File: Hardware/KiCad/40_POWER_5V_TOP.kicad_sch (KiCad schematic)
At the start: 0 parts

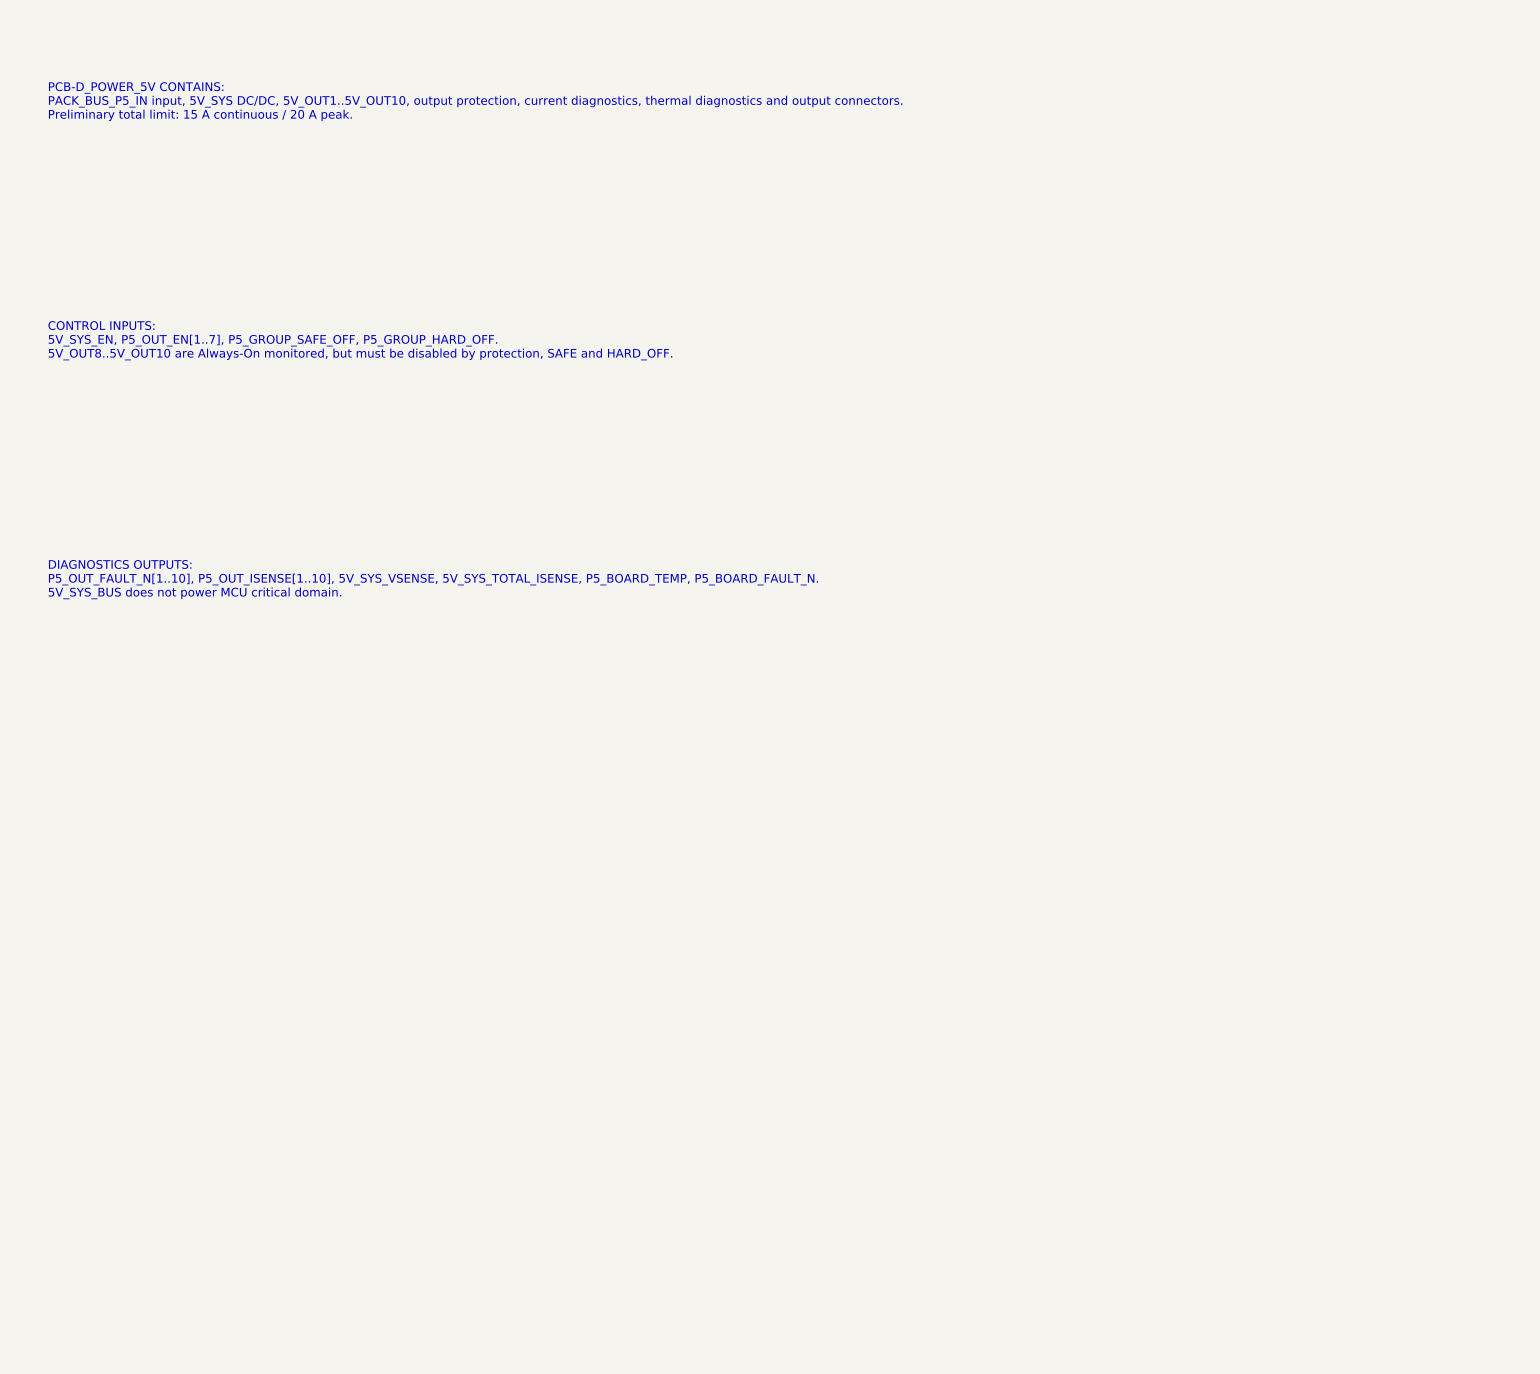
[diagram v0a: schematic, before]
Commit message: hardware: detail 40 power 5v top sheet
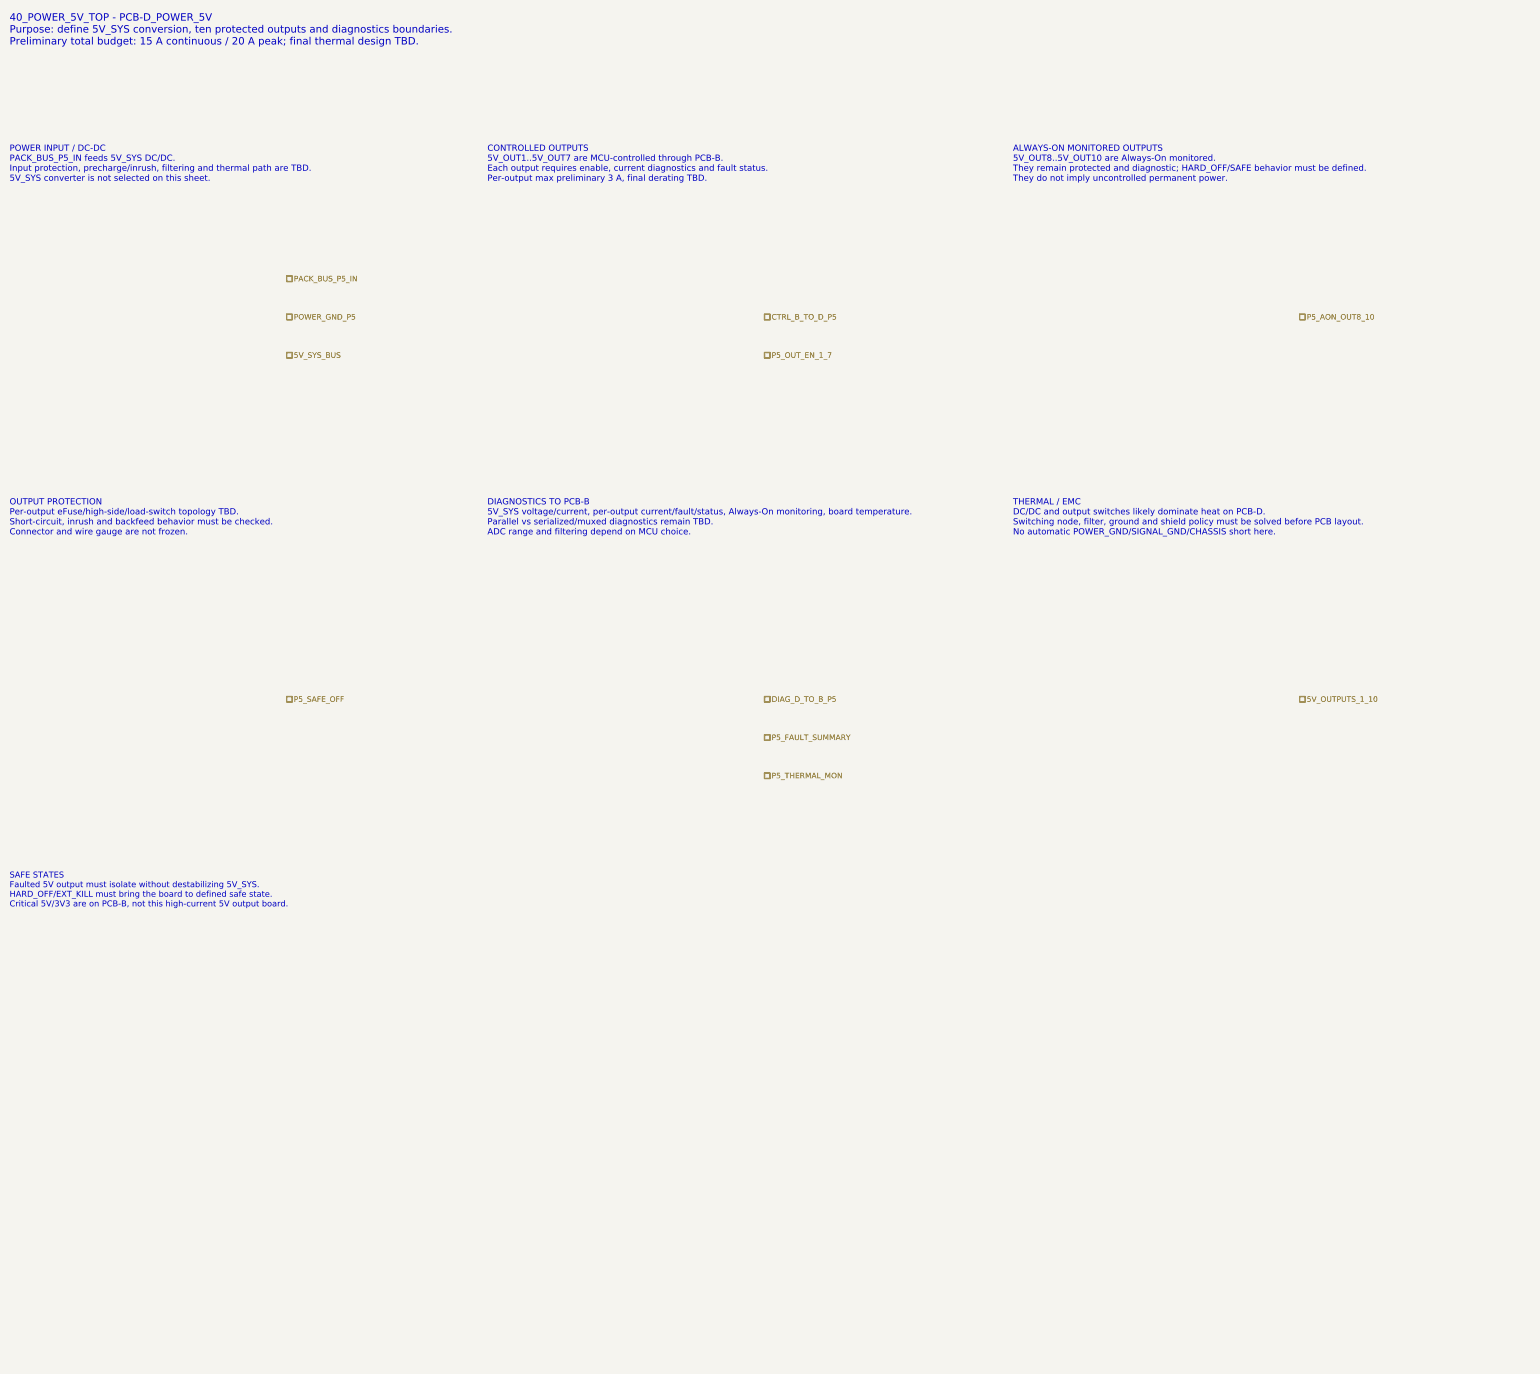
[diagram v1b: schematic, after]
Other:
- note added: "40_POWER_5V_TOP - PCB-D_POWER_5V Purpose: define 5V_SYS conversion, ten protected outputs and diagnostics boundaries. Preliminary total budget: 15 A continuous / 20 A peak; final thermal design TBD."
- note added: "ALWAYS-ON MONITORED OUTPUTS 5V_OUT8..5V_OUT10 are Always-On monitored. They remain protected and diagnostic; HARD_OFF/SAFE behavior must be defined. They do not imply uncontrolled permanent power."
- note added: "CONTROLLED OUTPUTS 5V_OUT1..5V_OUT7 are MCU-controlled through PCB-B. Each output requires enable, current diagnostics and fault status. Per-output max preliminary 3 A, final derating TBD."
- note added: "DIAGNOSTICS TO PCB-B 5V_SYS voltage/current, per-output current/fault/status, Always-On monitoring, board temperature. Parallel vs serialized/muxed diagnostics remain TBD. ADC range and filtering depend on MCU choice."
- note added: "OUTPUT PROTECTION Per-output eFuse/high-side/load-switch topology TBD. Short-circuit, inrush and backfeed behavior must be checked. Connector and wire gauge are not frozen."
- note added: "POWER INPUT / DC-DC PACK_BUS_P5_IN feeds 5V_SYS DC/DC. Input protection, precharge/inrush, filtering and thermal path are TBD. 5V_SYS converter is not selected on this sheet."
- note added: "SAFE STATES Faulted 5V output must isolate without destabilizing 5V_SYS. HARD_OFF/EXT_KILL must bring the board to defined safe state. Critical 5V/3V3 are on PCB-B, not this high-current 5V output board."
- note added: "THERMAL / EMC DC/DC and output switches likely dominate heat on PCB-D. Switching node, filter, ground and shield policy must be solved before PCB layout. No automatic POWER_GND/SIGNAL_GND/CHASSIS short here."
- note removed: "CONTROL INPUTS: 5V_SYS_EN, P5_OUT_EN[1..7], P5_GROUP_SAFE_OFF, P5_GROUP_HARD_OFF. 5V_OUT8..5V_OUT10 are Always-On monitored, but must be disabled by protection, SAFE and HARD_OFF."
- note removed: "DIAGNOSTICS OUTPUTS: P5_OUT_FAULT_N[1..10], P5_OUT_ISENSE[1..10], 5V_SYS_VSENSE, 5V_SYS_TOTAL_ISENSE, P5_BOARD_TEMP, P5_BOARD_FAULT_N. 5V_SYS_BUS does not power MCU critical domain."
- note removed: "PCB-D_POWER_5V CONTAINS: PACK_BUS_P5_IN input, 5V_SYS DC/DC, 5V_OUT1..5V_OUT10, output protection, current diagnostics, thermal diagnostics and output connectors. Preliminary total limit: 15 A continuous / 20 A peak."
- company: (none) -> Gonoboben/plataVM
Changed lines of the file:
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@@
 	(title_block
 		(title "40_POWER_5V_TOP - PCB-D_POWER_5V")
-		(date "2026-07-14")
-		(rev "A0")
-		(comment 1 "5V_SYS DC/DC and ten protected 5V outputs")
+		(date "2026-07-15")
+		(rev "A1")
+		(company "Gonoboben/plataVM")
+		(comment 1 "Architecture Level A: 5V_SYS DC/DC and ten 5V outputs")
+		(comment 2 "No DC/DC/eFuse part numbers or footprints selected")
 	)
-	(text "CONTROL INPUTS:\n5V_SYS_EN, P5_OUT_EN[1..7], P5_GROUP_SAFE_OFF, P5_GROUP_HARD_OFF.\n5V_OUT8..5V_OUT10 are Always-On monitored, but must be disabled by protection, SAFE and HARD_OFF."
+	(text "40_POWER_5V_TOP - PCB-D_POWER_5V\nPurpose: define 5V_SYS conversion, ten protected outputs and diagnostics boundaries.\nPreliminary total budget: 15 A continuous / 20 A peak; final thermal design TBD."
 		(exclude_from_sim no)
-		(at 20 75 0)
-		(effects
-			(font
-				(size 1.8 1.8)
-			)
-			(justify left)
-		)
+		(at 12 10 0)
+		(effects (font (size 1.55 1.55)) (justify left))
+		(uuid "p5-text-0001")
 	)
-	(text "DIAGNOSTICS OUTPUTS:\nP5_OUT_FAULT_N[1..10], P5_OUT_ISENSE[1..10], 5V_SYS_VSENSE, 5V_SYS_TOTAL_ISENSE, P5_BOARD_TEMP, P5_BOARD_FAULT_N.\n5V_SYS_BUS does not power MCU critical domain."
+	(text "POWER INPUT / DC-DC\nPACK_BUS_P5_IN feeds 5V_SYS DC/DC.\nInput protection, precharge/inrush, filtering and thermal path are TBD.\n5V_SYS converter is not selected on this sheet."
 		(exclude_from_sim no)
-		(at 20 125 0)
-		(effects
-			(font
-				(size 1.8 1.8)
-			)
-			(justify left)
-		)
+		(at 12 38 0)
+		(effects (font (size 1.3 1.3)) (justify left))
+		(uuid "p5-text-0002")
 	)
-	(text "PCB-D_POWER_5V CONTAINS:\nPACK_BUS_P5_IN input, 5V_SYS DC/DC, 5V_OUT1..5V_OUT10, output protection, current diagnostics, thermal diagnostics and output connectors.\nPreliminary total limit: 15 A continuous / 20 A peak."
+	(text "CONTROLLED OUTPUTS\n5V_OUT1..5V_OUT7 are MCU-controlled through PCB-B.\nEach output requires enable, current diagnostics and fault status.\nPer-output max preliminary 3 A, final derating TBD."
 		(exclude_from_sim no)
-		(at 20 25 0)
-		(effects
-			(font
-				(size 1.8 1.8)
-			)
-			(justify left)
-		)
+		(at 112 38 0)
+		(effects (font (size 1.3 1.3)) (justify left))
+		(uuid "p5-text-0003")
 	)
+	(text "ALWAYS-ON MONITORED OUTPUTS\n5V_OUT8..5V_OUT10 are Always-On monitored.\nThey remain protected and diagnostic; HARD_OFF/SAFE behavior must be defined.\nThey do not imply uncontrolled permanent power."
+		(exclude_from_sim no)
+		(at 222 38 0)
+		(effects (font (size 1.3 1.3)) (justify left))
+		(uuid "p5-text-0004")
+	)
+	(text "OUTPUT PROTECTION\nPer-output eFuse/high-side/load-switch topology TBD.\nShort-circuit, inrush and backfeed behavior must be checked.\nConnector and wire gauge are not frozen."
+		(exclude_from_sim no)
+		(at 12 112 0)
+		(effects (font (size 1.3 1.3)) (justify left))
+		(uuid "p5-text-0005")
+	)
+	(text "DIAGNOSTICS TO PCB-B\n5V_SYS voltage/current, per-output current/fault/status, Always-On monitoring, board temperature.\nParallel vs serialized/muxed diagnostics remain TBD.\nADC range and filtering depend on MCU choice."
+		(exclude_from_sim no)
+		(at 112 112 0)
+		(effects (font (size 1.3 1.3)) (justify left))
+		(uuid "p5-text-0006")
+	)
+	(text "THERMAL / EMC\nDC/DC and output switches likely dominate heat on PCB-D.\nSwitching node, filter, ground and shield policy must be solved before PCB layout.\nNo automatic POWER_GND/SIGNAL_GND/CHASSIS short here."
+		(exclude_from_sim no)
+		(at 222 112 0)
+		(effects (font (size 1.3 1.3)) (justify left))
+		(uuid "p5-text-0007")
+	)
+	(text "SAFE STATES\nFaulted 5V output must isolate without destabilizing 5V_SYS.\nHARD_OFF/EXT_KILL must bring the board to defined safe state.\nCritical 5V/3V3 are on PCB-B, not this high-current 5V output board."
+		(exclude_from_sim no)
+		(at 12 190 0)
+		(effects (font (size 1.25 1.25)) (justify left))
+		(uuid "p5-text-0008")
+	)
+	(hierarchical_label "PACK_BUS_P5_IN" (shape passive) (exclude_from_sim no) (at 70 62 0) (effects (font (size 1.15 1.15)) (justify left)) (uuid "p5-label-0001"))
+	(hierarchical_label "POWER_GND_P5" (shape passive) (exclude_from_sim no) (at 70 70 0) (effects (font (size 1.15 1.15)) (justify left)) (uuid "p5-label-0002"))
+	(hierarchical_label "5V_SYS_BUS" (shape passive) (exclude_from_sim no) (at 70 78 0) (effects (font (size 1.15 1.15)) (justify left)) (uuid "p5-label-0003"))
+	(hierarchical_label "CTRL_B_TO_D_P5" (shape passive) (exclude_from_sim no) (at 170 70 0) (effects (font (size 1.15 1.15)) (justify left)) (uuid "p5-label-0004"))
+	(hierarchical_label "P5_OUT_EN_1_7" (shape passive) (exclude_from_sim no) (at 170 78 0) (effects (font (size 1.15 1.15)) (justify left)) (uuid "p5-label-0005"))
+	(hierarchical_label "P5_AON_OUT8_10" (shape passive) (exclude_from_sim no) (at 282 70 0) (effects (font (size 1.15 1.15)) (justify left)) (uuid "p5-label-0006"))
+	(hierarchical_label "5V_OUTPUTS_1_10" (shape passive) (exclude_from_sim no) (at 282 150 0) (effects (font (size 1.15 1.15)) (justify left)) (uuid "p5-label-0007"))
+	(hierarchical_label "DIAG_D_TO_B_P5" (shape passive) (exclude_from_sim no) (at 170 150 0) (effects (font (size 1.15 1.15)) (justify left)) (uuid "p5-label-0008"))
+	(hierarchical_label "P5_FAULT_SUMMARY" (shape passive) (exclude_from_sim no) (at 170 158 0) (effects (font (size 1.15 1.15)) (justify left)) (uuid "p5-label-0009"))
+	(hierarchical_label "P5_SAFE_OFF" (shape passive) (exclude_from_sim no) (at 70 150 0) (effects (font (size 1.15 1.15)) (justify left)) (uuid "p5-label-0010"))
+	(hierarchical_label "P5_THERMAL_MON" (shape passive) (exclude_from_sim no) (at 170 166 0) (effects (font (size 1.15 1.15)) (justify left)) (uuid "p5-label-0011"))
 )
